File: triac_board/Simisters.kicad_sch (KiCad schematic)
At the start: 31 parts, among them J2 DG245-5.0-02P, J3 DG245-5.0-02P, J4 DG245-5.0-02P, J5 DG245-5.0-02P, J6 DG245-5.0-04P, U5 74AHCT1G14GW,125

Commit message: Triak v2.1
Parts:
- C15, C16: value 0,1uF 50V 0805 -> 0,1uF 100V 0603; footprint Capacitor_SMD:C_0805_2012Metric_Pad1.18x1.45mm_HandSolder -> Capacitor_SMD:C_0603_1608Metric
- J2, J3, J4, J5: value DG245-5.0-02P -> DG245-5.0-02P-11-00A(H)
- J6: value DG245-5.0-04P -> DG245-5.0-04P-11-00Z
- OC1: value FOD814 -> FOD814 (DIP-4)
- U5: value 74AHCT1G14GW,125 -> 74AHCT1G14GW,125 (SOT-23-5)

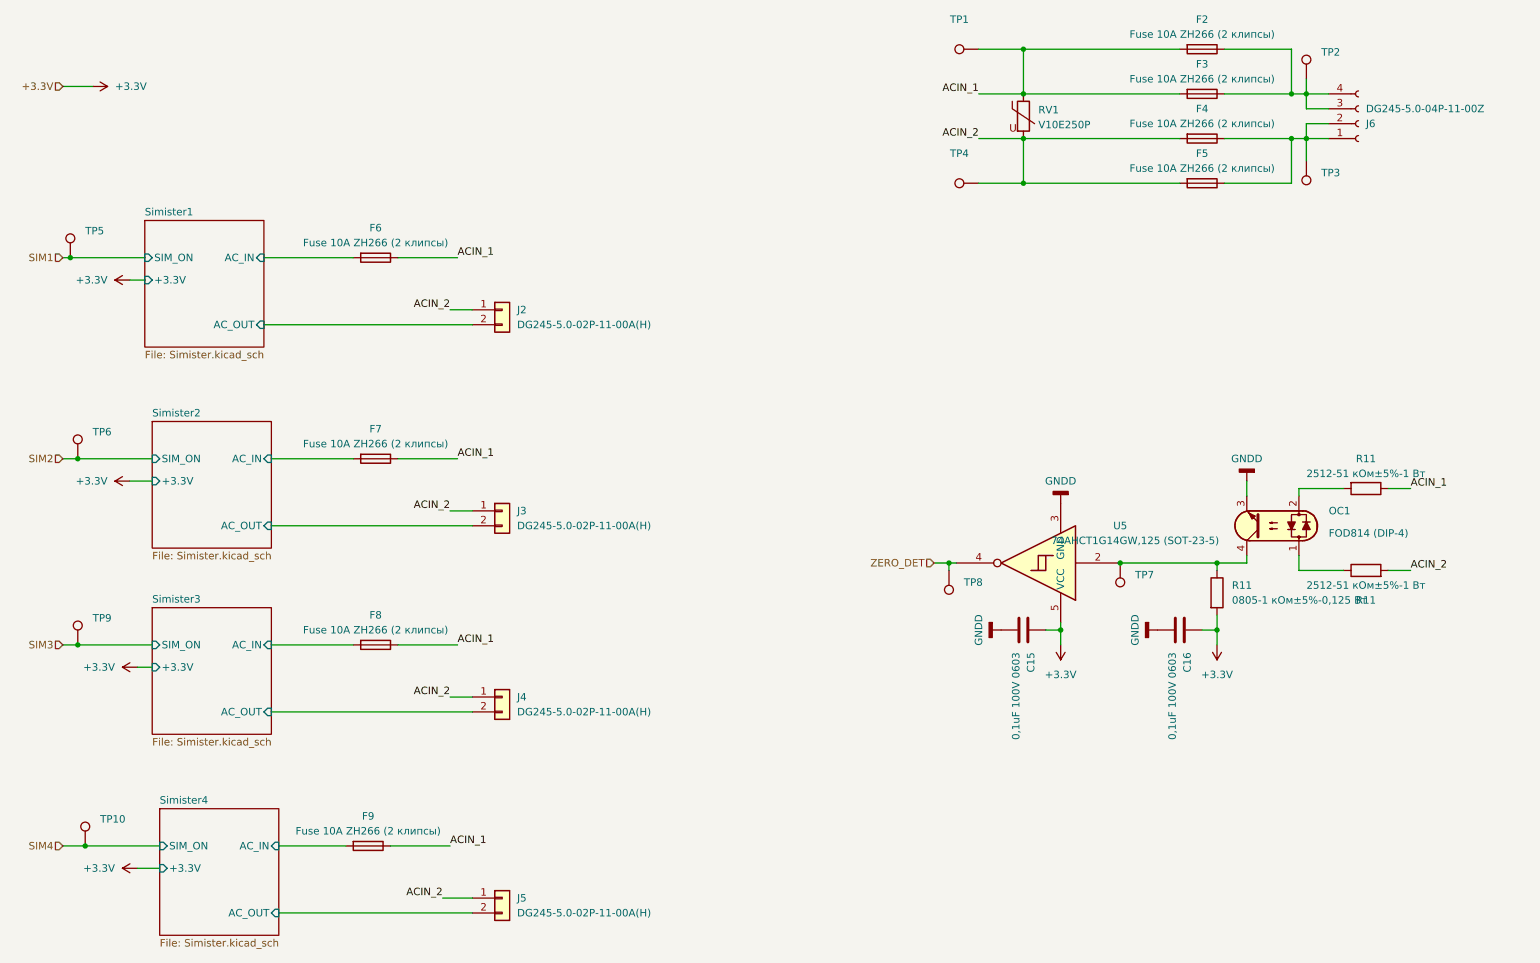
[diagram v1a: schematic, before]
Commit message: triak уменьшение нагрева
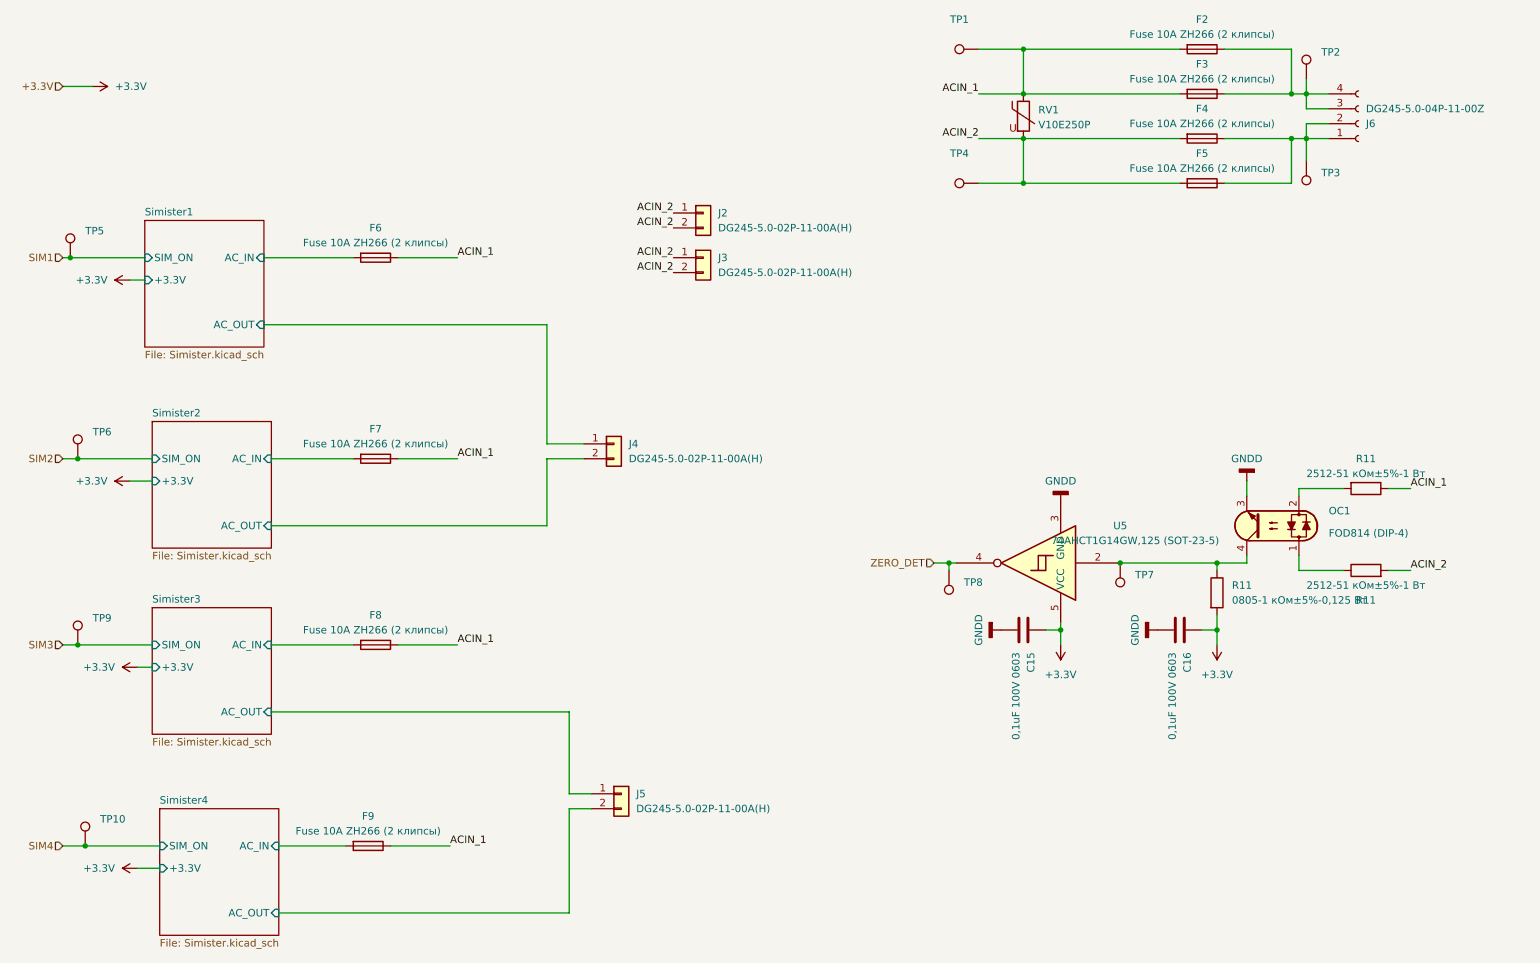
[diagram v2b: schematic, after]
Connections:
- net ACIN_2: now also J2.2 (Pin_2), J3.2 (Pin_2); no longer J4.1 (Pin_1), J5.1 (Pin_1)
- net Simister1/AC_OUT: now also J4.1 (Pin_1); no longer J2.2 (Pin_2)
- net Simister2/AC_OUT: now also J4.2 (Pin_2); no longer J3.2 (Pin_2)
- net Simister3/AC_OUT: now also J5.1 (Pin_1); no longer J4.2 (Pin_2)
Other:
- moved on the sheet: J2, J3, J4, J5
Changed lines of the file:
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@@
-    (stroke (width 0) (type default))
-  )
-  (wire (pts (xy 67.31 101.6) (xy 101.6 101.6))
     (stroke (width 0) (type default))
   )
@@
     (stroke (width 0) (type default))
   )
+  (wire (pts (xy 67.31 133.35) (xy 118.11 133.35))
+    (stroke (width 0) (type default))
+  )
+  (wire (pts (xy 114.3 67.31) (xy 114.3 87.63))
+    (stroke (width 0) (type default))
+  )
   (wire (pts (xy 195.58 43.18) (xy 195.58 35.56))
     (stroke (width 0) (type default))
@@
     (stroke (width 0) (type default))
   )
-  (wire (pts (xy 97.79 64.77) (xy 101.6 64.77))
-    (stroke (width 0) (type default))
-  )
   (wire (pts (xy 182.88 107.95) (xy 184.15 107.95))
     (stroke (width 0) (type default))
@@
     (stroke (width 0) (type default))
   )
+  (wire (pts (xy 118.11 147.32) (xy 121.92 147.32))
+    (stroke (width 0) (type default))
+  )
   (wire (pts (xy 201.93 119.38) (xy 201.93 121.92))
     (stroke (width 0) (type default))
   )
+  (wire (pts (xy 114.3 101.6) (xy 114.3 90.17))
+    (stroke (width 0) (type default))
+  )
   (wire (pts (xy 241.3 43.18) (xy 241.3 35.56))
     (stroke (width 0) (type default))
@@
     (stroke (width 0) (type default))
   )
+  (wire (pts (xy 114.3 90.17) (xy 120.65 90.17))
+    (stroke (width 0) (type default))
+  )
   (wire (pts (xy 228.6 119.38) (xy 228.6 121.92))
     (stroke (width 0) (type default))
@@
     (stroke (width 0) (type default))
   )
-  (wire (pts (xy 67.31 133.35) (xy 101.6 133.35))
+  (wire (pts (xy 67.31 101.6) (xy 114.3 101.6))
     (stroke (width 0) (type default))
   )
@@
     (stroke (width 0) (type default))
   )
-  (wire (pts (xy 66.04 67.31) (xy 101.6 67.31))
-    (stroke (width 0) (type default))
-  )
-  (wire (pts (xy 97.79 99.06) (xy 101.6 99.06))
-    (stroke (width 0) (type default))
-  )
   (wire (pts (xy 229.87 35.56) (xy 241.3 35.56))
     (stroke (width 0) (type default))
   )
+  (wire (pts (xy 118.11 167.64) (xy 118.11 149.86))
+    (stroke (width 0) (type default))
+  )
+  (wire (pts (xy 118.11 149.86) (xy 121.92 149.86))
+    (stroke (width 0) (type default))
+  )
   (wire (pts (xy 187.96 43.18) (xy 195.58 43.18))
     (stroke (width 0) (type default))
   )
+  (wire (pts (xy 68.58 167.64) (xy 118.11 167.64))
+    (stroke (width 0) (type default))
+  )
   (wire (pts (xy 43.18 93.98) (xy 46.99 93.98))
     (stroke (width 0) (type default))
@@
     (stroke (width 0) (type default))
   )
-  (wire (pts (xy 101.6 165.1) (xy 96.52 165.1))
-    (stroke (width 0) (type default))
-  )
   (wire (pts (xy 241.3 20.32) (xy 241.3 27.94))
     (stroke (width 0) (type default))
@@
     (stroke (width 0) (type default))
   )
-  (wire (pts (xy 68.58 167.64) (xy 101.6 167.64))
-    (stroke (width 0) (type default))
-  )
   (wire (pts (xy 67.31 90.17) (xy 81.28 90.17))
     (stroke (width 0) (type default))
@@
     (stroke (width 0) (type default))
   )
+  (wire (pts (xy 118.11 133.35) (xy 118.11 147.32))
+    (stroke (width 0) (type default))
+  )
   (wire (pts (xy 257.81 95.25) (xy 261.62 95.25))
     (stroke (width 0) (type default))
@@
     (stroke (width 0) (type default))
   )
+  (wire (pts (xy 114.3 87.63) (xy 120.65 87.63))
+    (stroke (width 0) (type default))
+  )
   (wire (pts (xy 187.96 27.94) (xy 195.58 27.94))
     (stroke (width 0) (type default))
@@
     (stroke (width 0) (type default))
   )
-  (wire (pts (xy 101.6 130.81) (xy 97.79 130.81))
-    (stroke (width 0) (type default))
-  )
   (wire (pts (xy 195.58 27.94) (xy 222.25 27.94))
     (stroke (width 0) (type default))
   )
+  (wire (pts (xy 66.04 67.31) (xy 114.3 67.31))
+    (stroke (width 0) (type default))
+  )
   (wire (pts (xy 228.6 116.84) (xy 228.6 119.38))
     (stroke (width 0) (type default))
@@
     (stroke (width 0) (type default))
   )
-  (label "ACIN_2" (at 97.79 64.77 180) (fields_autoplaced)
-    (effects (font (size 1.27 1.27)) (justify right bottom))
-  )
-  (label "ACIN_2" (at 96.52 165.1 180) (fields_autoplaced)
+  (label "ACIN_2" (at 135.89 48.26 180) (fields_autoplaced)
     (effects (font (size 1.27 1.27)) (justify right bottom))
   )
@@
     (effects (font (size 1.27 1.27)) (justify right bottom))
   )
+  (label "ACIN_2" (at 135.89 58.42 180) (fields_autoplaced)
+    (effects (font (size 1.27 1.27)) (justify right bottom))
+  )
   (label "ACIN_1" (at 97.79 156.21 0) (fields_autoplaced)
     (effects (font (size 1.27 1.27)) (justify left bottom))
@@
     (effects (font (size 1.27 1.27)) (justify left bottom))
   )
-  (label "ACIN_2" (at 97.79 99.06 180) (fields_autoplaced)
+  (label "ACIN_2" (at 135.89 50.8 180) (fields_autoplaced)
+    (effects (font (size 1.27 1.27)) (justify right bottom))
+  )
+  (label "ACIN_2" (at 135.89 55.88 180) (fields_autoplaced)
     (effects (font (size 1.27 1.27)) (justify right bottom))
   )
@@
     (effects (font (size 1.27 1.27)) (justify left bottom))
   )
-  (label "ACIN_2" (at 97.79 130.81 180) (fields_autoplaced)
-    (effects (font (size 1.27 1.27)) (justify right bottom))
-  )
   (label "ACIN_1" (at 187.96 27.94 180) (fields_autoplaced)
     (effects (font (size 1.27 1.27)) (justify right bottom))
@@
     )
   )
-  (symbol (lib_id "Connector_Generic:Conn_01x02") (at 106.68 99.06 0) (unit 1)
+  (symbol (lib_id "Connector_Generic:Conn_01x02") (at 140.97 55.88 0) (unit 1)
     (in_bom yes) (on_board yes) (dnp no)
-    (property "Reference" "J3" (at 109.22 99.06 0)
-      (effects (font (size 1.27 1.27)) (justify left))
-    )
-    (property "Value" "DG245-5.0-02P-11-00A(H)" (at 109.22 101.6 0)
-      (effects (font (size 1.27 1.27)) (justify left))
-    )
-    (property "Footprint" "Connector:DG245-5.0-02P" (at 106.68 99.06 0)
-      (effects (font (size 1.27 1.27)) hide)
-    )
-    (property "Datasheet" "~" (at 106.68 99.06 0)
+    (property "Reference" "J3" (at 143.51 55.88 0)
+      (effects (font (size 1.27 1.27)) (justify left))
+    )
+    (property "Value" "DG245-5.0-02P-11-00A(H)" (at 143.51 58.42 0)
+      (effects (font (size 1.27 1.27)) (justify left))
+    )
+    (property "Footprint" "Connector:DG245-5.0-02P" (at 140.97 55.88 0)
+      (effects (font (size 1.27 1.27)) hide)
+    )
+    (property "Datasheet" "~" (at 140.97 55.88 0)
       (effects (font (size 1.27 1.27)) hide)
     )
@@
     )
   )
-  (symbol (lib_id "Connector_Generic:Conn_01x02") (at 106.68 130.81 0) (unit 1)
+  (symbol (lib_id "Connector_Generic:Conn_01x02") (at 125.73 87.63 0) (unit 1)
     (in_bom yes) (on_board yes) (dnp no)
-    (property "Reference" "J4" (at 109.22 130.81 0)
-      (effects (font (size 1.27 1.27)) (justify left))
-    )
-    (property "Value" "DG245-5.0-02P-11-00A(H)" (at 109.22 133.35 0)
-      (effects (font (size 1.27 1.27)) (justify left))
-    )
-    (property "Footprint" "Connector:DG245-5.0-02P" (at 106.68 130.81 0)
-      (effects (font (size 1.27 1.27)) hide)
-    )
-    (property "Datasheet" "~" (at 106.68 130.81 0)
+    (property "Reference" "J4" (at 128.27 87.63 0)
+      (effects (font (size 1.27 1.27)) (justify left))
+    )
+    (property "Value" "DG245-5.0-02P-11-00A(H)" (at 128.27 90.17 0)
+      (effects (font (size 1.27 1.27)) (justify left))
+    )
+    (property "Footprint" "Connector:DG245-5.0-02P" (at 125.73 87.63 0)
+      (effects (font (size 1.27 1.27)) hide)
+    )
+    (property "Datasheet" "~" (at 125.73 87.63 0)
       (effects (font (size 1.27 1.27)) hide)
     )
@@
     )
   )
-  (symbol (lib_id "Connector_Generic:Conn_01x02") (at 106.68 165.1 0) (unit 1)
+  (symbol (lib_id "Connector_Generic:Conn_01x02") (at 127 147.32 0) (unit 1)
     (in_bom yes) (on_board yes) (dnp no)
-    (property "Reference" "J5" (at 109.22 165.1 0)
-      (effects (font (size 1.27 1.27)) (justify left))
-    )
-    (property "Value" "DG245-5.0-02P-11-00A(H)" (at 109.22 167.64 0)
-      (effects (font (size 1.27 1.27)) (justify left))
-    )
-    (property "Footprint" "Connector:DG245-5.0-02P" (at 106.68 165.1 0)
-      (effects (font (size 1.27 1.27)) hide)
-    )
-    (property "Datasheet" "~" (at 106.68 165.1 0)
+    (property "Reference" "J5" (at 129.54 147.32 0)
+      (effects (font (size 1.27 1.27)) (justify left))
+    )
+    (property "Value" "DG245-5.0-02P-11-00A(H)" (at 129.54 149.86 0)
+      (effects (font (size 1.27 1.27)) (justify left))
+    )
+    (property "Footprint" "Connector:DG245-5.0-02P" (at 127 147.32 0)
+      (effects (font (size 1.27 1.27)) hide)
+    )
+    (property "Datasheet" "~" (at 127 147.32 0)
       (effects (font (size 1.27 1.27)) hide)
     )
@@
     )
   )
-  (symbol (lib_id "Connector_Generic:Conn_01x02") (at 106.68 64.77 0) (unit 1)
+  (symbol (lib_id "Connector_Generic:Conn_01x02") (at 140.97 48.26 0) (unit 1)
     (in_bom yes) (on_board yes) (dnp no)
-    (property "Reference" "J2" (at 109.22 64.77 0)
-      (effects (font (size 1.27 1.27)) (justify left))
-    )
-    (property "Value" "DG245-5.0-02P-11-00A(H)" (at 109.22 67.31 0)
-      (effects (font (size 1.27 1.27)) (justify left))
-    )
-    (property "Footprint" "Connector:DG245-5.0-02P" (at 106.68 64.77 0)
-      (effects (font (size 1.27 1.27)) hide)
-    )
-    (property "Datasheet" "~" (at 106.68 64.77 0)
-      (effects (font (size 1.27 1.27)) hide)
-    )
+    (property "Reference" "J2" (at 143.51 48.26 0)
+      (effects (font (size 1.27 1.27)) (justify left))
+    )
+    (property "Value" "DG245-5.0-02P-11-00A(H)" (at 143.51 50.8 0)
+      (effects (font (size 1.27 1.27)) (justify left))
+    )
+    (property "Footprint" "Connector:DG245-5.0-02P" (at 140.97 48.26 0)
+      (effects (font (size 1.27 1.27)) hide)
+    )
+    (property "Datasheet" "~" (at 140.97 48.26 0)
+      (effects (font (size 1.27 1.27)) hide)
+    )

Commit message: triak убраны тестовые площадки с 220в
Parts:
- removed TP1, TP2, TP3, TP4: TestPoint, PCM_4ms_TestPoint:TestPoint_D1, symbol Connector:TestPoint
- R11: footprint PCM_Resistor_SMD_AKL:R_2512_6332Metric -> Resistor_SMD:R_2512_6332Metric

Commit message: update schemas
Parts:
- U5: value 74AHCT1G14GW,125 (SOT-23-5) -> 74AHCT1G14GV,125 (SOT-23-5)
- renumbered R11 to R10, R11 to R9
